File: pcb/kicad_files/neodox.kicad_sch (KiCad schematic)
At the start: 76 parts, among them K0 KEYSW, K1 KEYSW, K10 KEYSW, K11 KEYSW, K12 KEYSW, K13 KEYSW, K14 KEYSW, K15 KEYSW, K16 KEYSW, K2 KEYSW, K20 KEYSW, K21 KEYSW, K22 KEYSW, K23 KEYSW, K24 KEYSW, K25 KEYSW, K26 KEYSW, K3 KEYSW, K30 KEYSW, K31 KEYSW, K32 KEYSW, K33 KEYSW, K34 KEYSW, K35 KEYSW, K36 KEYSW, K4 KEYSW, K40 KEYSW, K41 KEYSW, K42 KEYSW, K43 KEYSW, K44 KEYSW, K45 KEYSW, K46 KEYSW, K5 KEYSW, K6 KEYSW, U1 ProMicro

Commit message: add cutout
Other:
- title: Redox keyboard -> Neodox keyboard
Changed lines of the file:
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@@
   (paper "A4")
   (title_block
-    (title "Redox keyboard")
+    (title "Neodox keyboard")
     (date "2018-05-05")
     (rev "1.0")
-    (comment 1 "designed by Mattia Dal Ben")
-    (comment 2 "https://github.com/mattdibi/redox-keyboard")
+    (comment 1 "designed by Mattia Dal Ben, remixed by Pastitas")
+    (comment 2 "https://github.com/pastitas/neodox-keyboard")
   )
   (junction (at 218.44 67.31) (diameter 0) (color 0 0 0 0)

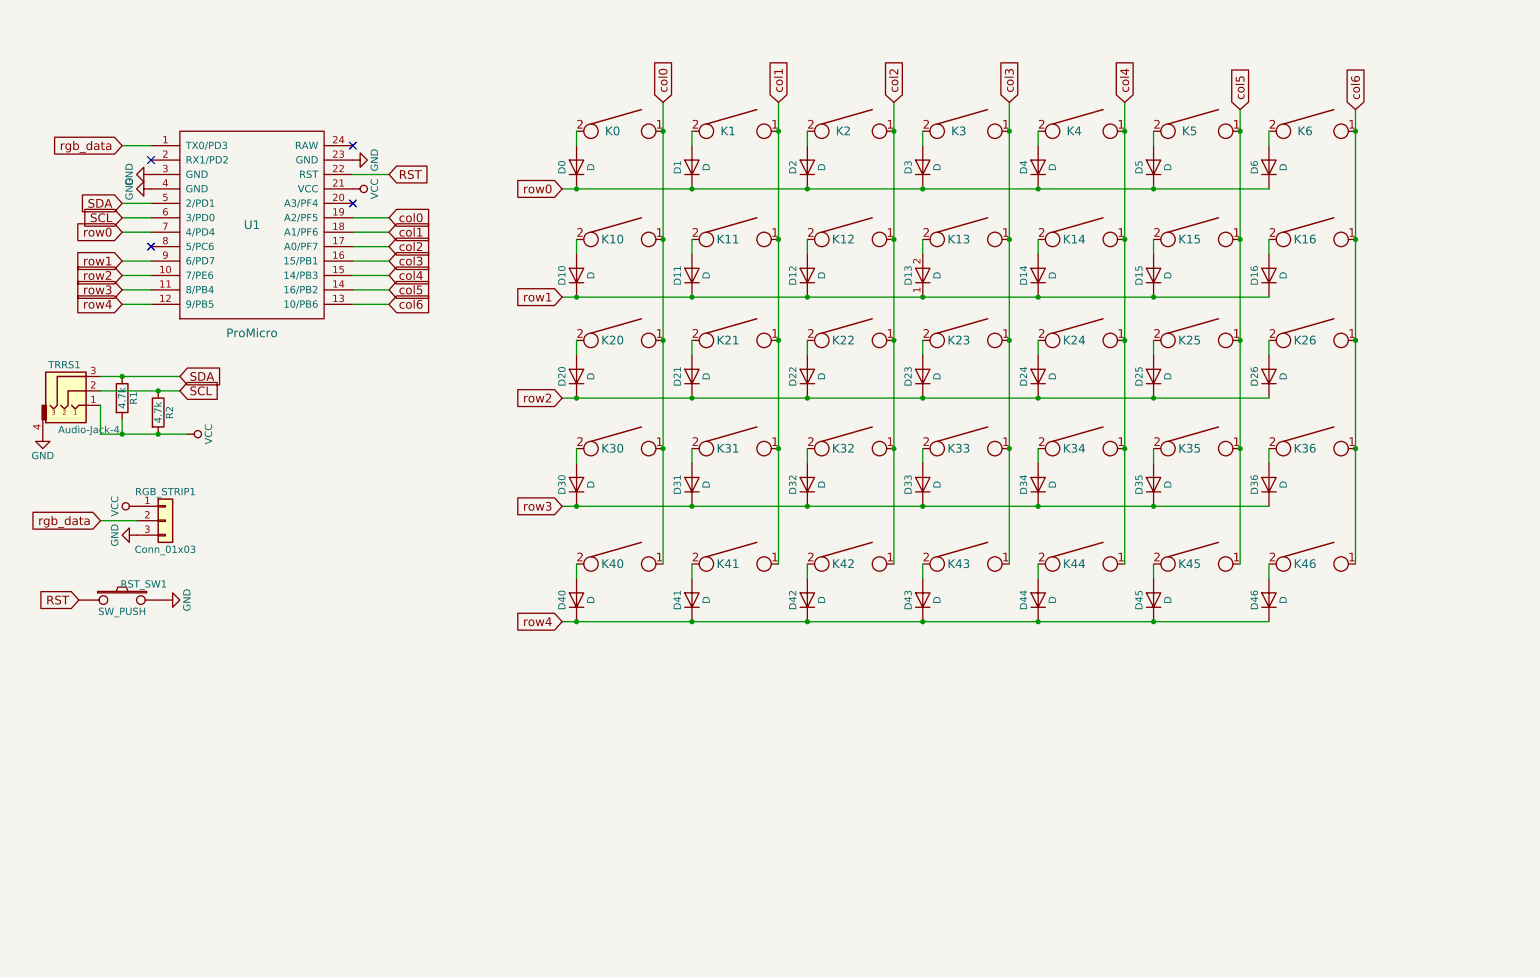
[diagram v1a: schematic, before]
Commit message: add all features and board layout, pending routing
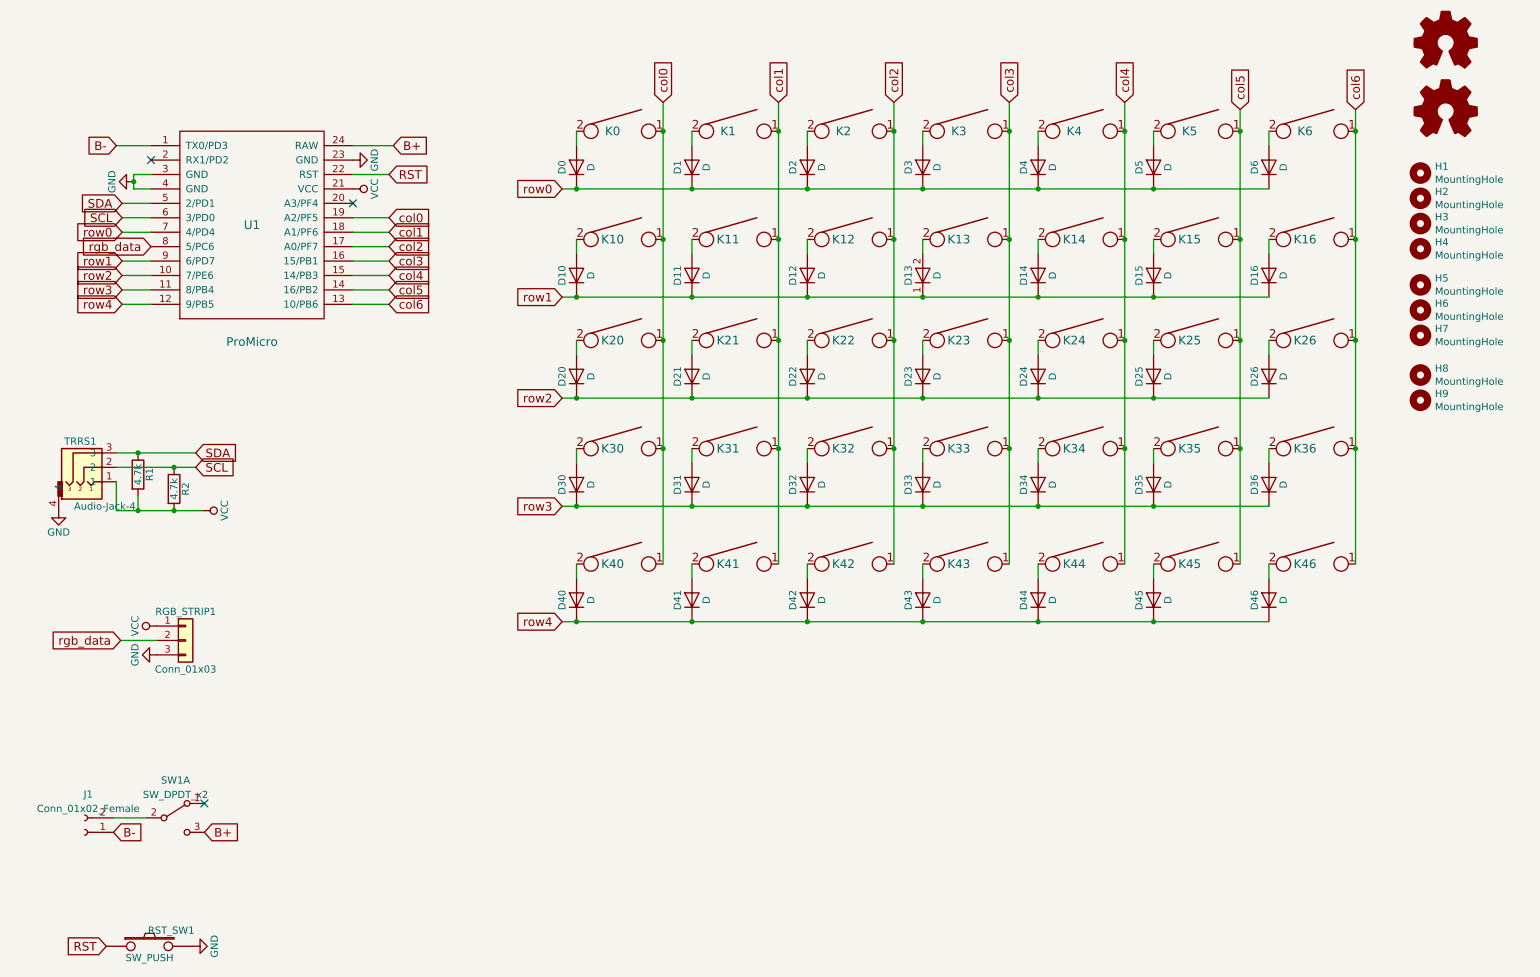
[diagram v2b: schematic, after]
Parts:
- added G1, G2: Logo_Open_Hardware_Small, kbd:corne, symbol Graphic:Logo_Open_Hardware_Small
- added H1, H2, H3, H4, H5, H6, H7, H8, H9: MountingHole, kbd:LEGO_HOLE, symbol Mechanical:MountingHole
- added J1: Conn_01x02_Female, Connector_PinHeader_1.27mm:PinHeader_1x02_P1.27mm_Vertical, symbol Connector:Conn_01x02_Female
- added SW1: SW_DPDT_x2, Keyboard_reversible:switch_reversible, symbol Switch:SW_DPDT_x2
- R1, R2: footprint Keebio-Parts:Resistor-Compact -> Keyboard_reversible:Resistor-Hybrid
- RGB_STRIP1: footprint Pin_Headers:Pin_Header_Straight_1x03_Pitch2.54mm -> Connector_PinHeader_1.27mm:PinHeader_1x03_P1.27mm_Vertical
- RST_SW1: footprint Buttons_Switches_ThroughHole:SW_PUSH_6mm_h4.3mm -> Keyboard_reversible:pushbutton_reversible
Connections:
- net rgb_data: now also U1.8 (5/PC6); no longer U1.1 (TX0/PD3)
- net B+: now reaches U1.24 (RAW)
- net B+: now also SW1.3 (C)
- new net: J1.2 (Pin_2), SW1.2 (B)
- new net B-: J1.1 (Pin_1), U1.1 (TX0/PD3)
- no-connect marks 4 -> 3
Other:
- moved on the sheet: R1, R2, RGB_STRIP1, RST_SW1

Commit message: chchchchangeees
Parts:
- removed G1, G2: Logo_Open_Hardware_Small, kbd:corne, symbol Graphic:Logo_Open_Hardware_Small
- removed H5, H6, H7, H8, H9: MountingHole, kbd:LEGO_HOLE, symbol Mechanical:MountingHole
- D1: renamed from D0; footprint keyboard_reversible:Diode-dual -> Keyboard_reversible:Diode-dual
- D10: renamed from D12; footprint keyboard_reversible:Diode-dual -> Keyboard_reversible:Diode-dual
- D11: renamed from D13; footprint keyboard_reversible:Diode-dual -> Keyboard_reversible:Diode-dual
- D12: renamed from D14; footprint keyboard_reversible:Diode-dual -> Keyboard_reversible:Diode-dual
- D13: renamed from D15; footprint keyboard_reversible:Diode-dual -> Keyboard_reversible:Diode-dual
- D14: renamed from D16; footprint keyboard_reversible:Diode-dual -> Keyboard_reversible:Diode-dual
- D15: renamed from D20; footprint keyboard_reversible:Diode-dual -> Keyboard_reversible:Diode-dual
- D16: renamed from D21; footprint keyboard_reversible:Diode-dual -> Keyboard_reversible:Diode-dual
- D17: renamed from D22; footprint keyboard_reversible:Diode-dual -> Keyboard_reversible:Diode-dual
- D18: renamed from D23; footprint keyboard_reversible:Diode-dual -> Keyboard_reversible:Diode-dual
- D19: renamed from D24; footprint keyboard_reversible:Diode-dual -> Keyboard_reversible:Diode-dual
- D2: renamed from D1; footprint keyboard_reversible:Diode-dual -> Keyboard_reversible:Diode-dual
- D20: renamed from D25; footprint keyboard_reversible:Diode-dual -> Keyboard_reversible:Diode-dual
- D21: renamed from D26; footprint keyboard_reversible:Diode-dual -> Keyboard_reversible:Diode-dual
- D22: renamed from D30; footprint keyboard_reversible:Diode-dual -> Keyboard_reversible:Diode-dual
- D23: renamed from D31; footprint keyboard_reversible:Diode-dual -> Keyboard_reversible:Diode-dual
- D24: renamed from D32; footprint keyboard_reversible:Diode-dual -> Keyboard_reversible:Diode-dual
- D25: renamed from D33; footprint keyboard_reversible:Diode-dual -> Keyboard_reversible:Diode-dual
- D26: renamed from D34; footprint keyboard_reversible:Diode-dual -> Keyboard_reversible:Diode-dual
- D27: renamed from D35; footprint keyboard_reversible:Diode-dual -> Keyboard_reversible:Diode-dual
- D28: renamed from D36; footprint keyboard_reversible:Diode-dual -> Keyboard_reversible:Diode-dual
- D29: renamed from D40; footprint keyboard_reversible:Diode-dual -> Keyboard_reversible:Diode-dual
- D3: renamed from D2; footprint keyboard_reversible:Diode-dual -> Keyboard_reversible:Diode-dual
- D30: renamed from D41; footprint keyboard_reversible:Diode-dual -> Keyboard_reversible:Diode-dual
- D31: renamed from D42; footprint keyboard_reversible:Diode-dual -> Keyboard_reversible:Diode-dual
- D32: renamed from D43; footprint keyboard_reversible:Diode-dual -> Keyboard_reversible:Diode-dual
- D33: renamed from D44; footprint keyboard_reversible:Diode-dual -> Keyboard_reversible:Diode-dual
- D34: renamed from D45; footprint keyboard_reversible:Diode-dual -> Keyboard_reversible:Diode-dual
- D35: renamed from D46; footprint keyboard_reversible:Diode-dual -> Keyboard_reversible:Diode-dual
- D4: renamed from D3; footprint keyboard_reversible:Diode-dual -> Keyboard_reversible:Diode-dual
- D5: renamed from D4; footprint keyboard_reversible:Diode-dual -> Keyboard_reversible:Diode-dual
- D6: renamed from D5; footprint keyboard_reversible:Diode-dual -> Keyboard_reversible:Diode-dual
- D7: renamed from D6; footprint keyboard_reversible:Diode-dual -> Keyboard_reversible:Diode-dual
- D8: renamed from D10; footprint keyboard_reversible:Diode-dual -> Keyboard_reversible:Diode-dual
- D9: renamed from D11; footprint keyboard_reversible:Diode-dual -> Keyboard_reversible:Diode-dual
- H1, H2, H3, H4: footprint kbd:LEGO_HOLE -> MountingHole:MountingHole_3.2mm_M3
- U1: footprint keyboard_reversible:ProMicro -> Keyboard_reversible:ProMicro_unrouted
- renumbered K0 to S1, K12 to S10, K13 to S11, K14 to S12, K15 to S13, K16 to S14, K20 to S15, K21 to S16, K22 to S17, K23 to S18, K24 to S19, K1 to S2, K25 to S20, K26 to S21, K30 to S22, K31 to S23, K32 to S24, K33 to S25, K34 to S26, K35 to S27, K36 to S28, K40 to S29, K2 to S3, K41 to S30, K42 to S31, K43 to S32, K44 to S33, K45 to S34, K46 to S35, K3 to S4, K4 to S5, K5 to S6, K6 to S7, K10 to S8, K11 to S9

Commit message: Build and pcb changes
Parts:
- S1, S10, S11, S12, S13, S14, S15, S16, S17, S18, S19, S2, S20, S21, S22, S23, S24, S25, S26, S27, S28, S29, S3, S30, S31, S32, S33, S34, S35, S4, S5, S6, S7, S8, S9: footprint Keyboard_reversible:Kailh_socket_MX_optional_reversible -> keyboard_reversible:Kailh_socket_MX_optional_reversible

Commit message: Change name
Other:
- title: Neodox keyboard -> neo-redox keyboard
